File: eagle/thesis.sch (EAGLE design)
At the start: 18 parts, among them J1 RJ11-6PTH, U1 ITG-3200, U2 ADXL362

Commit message: wrote a bunch and added references and pictures
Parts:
- removed J1: RJ11-6PTH, SparkFun-Connectors:RJ11-6PTH
- removed U$4: SPARKFUN_HMC5883LSMD, HMC5883L_Breakout-v11:SPARKFUN_HMC5883LSMD
- added HMC5883L: SPARKFUN_HMC5883LSMD, HMC5883L_Breakout-v11:SPARKFUN_HMC5883LSMD
- added JHMR2300: RJ11-6PTH, SparkFun-Connectors:RJ11-6PTH
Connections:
- net 33V: now also C6.2, HMC5883L.S1, HMC5883L.VDD, HMC5883L.VDDIO, JHMR2300.2; no longer J1.2, U$4.S1, U$4.VDD, U$4.VDDIO
- net GND1_1: now also JHMR2300.1; no longer J1.1
- net GNDHEAD: now also HMC5883L.GND@1, HMC5883L.GND@2; no longer U$4.GND@1, U$4.GND@2
- net N$12: now also HMC5883L.C1; no longer U$4.C1
- net N$5: now also HMC5883L.SETP; no longer U$4.SETP
- net N$7: now also HMC5883L.SETC; no longer U$4.SETC
- net RX1: now also JHMR2300.3; no longer J1.3
- net SCL: now also HMC5883L.SCL; no longer U$4.SCL
- net SDA: now also HMC5883L.SDA; no longer U$4.SDA
- net TX1: now also JHMR2300.4; no longer J1.4
- net VIN: now also JHMR2300.5; no longer J1.5
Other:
- moved on the sheet: C1, C2, C3, C4, C5, C6, C7, R1, R2, U$3G$1, U1

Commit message: wrote more.
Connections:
- new net SCL1: U$1.SCL1, U1.SCL
- new net SDA1: U$1.SDA1, U1.SDA
- net 33V: now also JHMR2300.5; no longer JHMR2300.2
- net GND1_1: now also JHMR2300.6; no longer JHMR2300.1
- net RX1: now also JHMR2300.4; no longer JHMR2300.3
- net SCL: no longer U1.SCL
- net SDA: no longer U1.SDA
- net TX1: now also JHMR2300.3; no longer JHMR2300.4
- net VIN: now also JHMR2300.2; no longer JHMR2300.5
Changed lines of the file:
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@@
-</segment>
-<segment>
-<pinref part="JHMR2300" gate="G$1" pin="2"/>
-<wire x1="83.82" y1="78.74" x2="78.74" y2="78.74" width="0.1524" layer="91"/>
-<label x="81.28" y="78.74" size="1.778" layer="95" rot="R180"/>
 </segment>
 <segment>
@@
 <junction x="81.28" y="195.58"/>
 <label x="81.28" y="198.12" size="1.778" layer="95"/>
+</segment>
+<segment>
+<pinref part="JHMR2300" gate="G$1" pin="5"/>
+<wire x1="78.74" y1="86.36" x2="83.82" y2="86.36" width="0.1524" layer="91"/>
+<label x="76.2" y="86.36" size="1.778" layer="95"/>
 </segment>
 </net>
@@
 </segment>
 <segment>
-<pinref part="JHMR2300" gate="G$1" pin="5"/>
-<wire x1="83.82" y1="86.36" x2="78.74" y2="86.36" width="0.1524" layer="91"/>
-<label x="76.2" y="86.36" size="1.778" layer="95"/>
+<pinref part="JHMR2300" gate="G$1" pin="2"/>
+<wire x1="78.74" y1="78.74" x2="83.82" y2="78.74" width="0.1524" layer="91"/>
+<label x="76.2" y="78.74" size="1.778" layer="95"/>
 </segment>
 </net>
 <net name="TX1" class="0">
+<segment>
+<pinref part="U$1" gate="G$1" pin="TX1"/>
+<wire x1="-5.08" y1="45.72" x2="-2.54" y2="45.72" width="0.1524" layer="91"/>
+</segment>
+<segment>
+<pinref part="JHMR2300" gate="G$1" pin="3"/>
+<wire x1="83.82" y1="81.28" x2="78.74" y2="81.28" width="0.1524" layer="91"/>
+<label x="78.74" y="81.28" size="1.778" layer="95"/>
+</segment>
+</net>
+<net name="RX1" class="0">
+<segment>
+<pinref part="U$1" gate="G$1" pin="RX1"/>
+<wire x1="-2.54" y1="43.18" x2="-5.08" y2="43.18" width="0.1524" layer="91"/>
+</segment>
 <segment>
 <pinref part="JHMR2300" gate="G$1" pin="4"/>
 <wire x1="83.82" y1="83.82" x2="78.74" y2="83.82" width="0.1524" layer="91"/>
-<label x="81.28" y="83.82" size="1.778" layer="95" rot="R180"/>
-</segment>
-<segment>
-<pinref part="U$1" gate="G$1" pin="TX1"/>
-<wire x1="-5.08" y1="45.72" x2="-2.54" y2="45.72" width="0.1524" layer="91"/>
-</segment>
-</net>
-<net name="RX1" class="0">
-<segment>
-<pinref part="JHMR2300" gate="G$1" pin="3"/>
-<wire x1="78.74" y1="81.28" x2="83.82" y2="81.28" width="0.1524" layer="91"/>
-<label x="81.28" y="81.28" size="1.778" layer="95" rot="R180"/>
-</segment>
-<segment>
-<pinref part="U$1" gate="G$1" pin="RX1"/>
-<wire x1="-2.54" y1="43.18" x2="-5.08" y2="43.18" width="0.1524" layer="91"/>
+<label x="78.74" y="83.82" size="1.778" layer="95"/>
 </segment>
 </net>
@@
 <wire x1="-5.08" y1="58.42" x2="-2.54" y2="58.42" width="0.1524" layer="91"/>
 </segment>
-<segment>
-<pinref part="U1" gate="G$1" pin="SCL"/>
-<wire x1="50.8" y1="109.22" x2="45.72" y2="109.22" width="0.1524" layer="91"/>
-<label x="45.72" y="109.22" size="1.778" layer="95" rot="R180"/>
-</segment>
 </net>
 <net name="SDA" class="0">
@@
 <label x="2.54" y="157.48" size="1.778" layer="95" rot="R90"/>
 </segment>
-<segment>
-<pinref part="U1" gate="G$1" pin="SDA"/>
-<wire x1="50.8" y1="104.14" x2="45.72" y2="104.14" width="0.1524" layer="91"/>
-<label x="45.72" y="104.14" size="1.778" layer="95" rot="R180"/>
-</segment>
 </net>
 <net name="SCLK" class="0">
@@
 </segment>
 <segment>
-<pinref part="JHMR2300" gate="G$1" pin="1"/>
-<wire x1="83.82" y1="76.2" x2="78.74" y2="76.2" width="0.1524" layer="91"/>
-<label x="83.82" y="76.2" size="1.778" layer="95" rot="R180"/>
-</segment>
-<segment>
 <pinref part="U$6" gate="G$1" pin="GND"/>
 <wire x1="119.38" y1="76.2" x2="124.46" y2="76.2" width="0.1524" layer="91"/>
@@
 <wire x1="-7.62" y1="185.42" x2="-12.7" y2="185.42" width="0.1524" layer="91"/>
 <label x="-12.7" y="185.42" size="1.778" layer="95" rot="R180"/>
+</segment>
+<segment>
+<pinref part="JHMR2300" gate="G$1" pin="6"/>
+<wire x1="78.74" y1="88.9" x2="83.82" y2="88.9" width="0.1524" layer="91"/>
+<label x="76.2" y="88.9" size="1.778" layer="95"/>
 </segment>
 </net>
@@
 <pinref part="HMC5883L" gate="G$1" pin="GND@1"/>
 <wire x1="48.26" y1="175.26" x2="43.18" y2="175.26" width="0.1524" layer="91"/>
+<label x="40.64" y="175.26" size="1.778" layer="95"/>
 </segment>
 <segment>
 <pinref part="HMC5883L" gate="G$1" pin="GND@2"/>
 <wire x1="48.26" y1="172.72" x2="43.18" y2="172.72" width="0.1524" layer="91"/>
-</segment>
-</net>
+<label x="40.64" y="172.72" size="1.778" layer="95"/>
+</segment>
+</net>
+<net name="SCL1" class="0">
+<segment>
+<pinref part="U$1" gate="G$1" pin="SCL1"/>
+<wire x1="7.62" y1="86.36" x2="7.62" y2="91.44" width="0.1524" layer="91"/>
+</segment>
+<segment>
+<pinref part="U1" gate="G$1" pin="SCL"/>
+<wire x1="50.8" y1="109.22" x2="45.72" y2="109.22" width="0.1524" layer="91"/>
+<label x="45.72" y="109.22" size="1.778" layer="95" rot="R180"/>
+</segment>
+</net>
+<net name="SDA1" class="0">
+<segment>
+<pinref part="U$1" gate="G$1" pin="SDA1"/>
+<wire x1="10.16" y1="86.36" x2="10.16" y2="91.44" width="0.1524" layer="91"/>
+</segment>
+<segment>
+<pinref part="U1" gate="G$1" pin="SDA"/>
+<wire x1="50.8" y1="104.14" x2="45.72" y2="104.14" width="0.1524" layer="91"/>
+<label x="45.72" y="104.14" size="1.778" layer="95" rot="R180"/>
+</segment>
+</net>

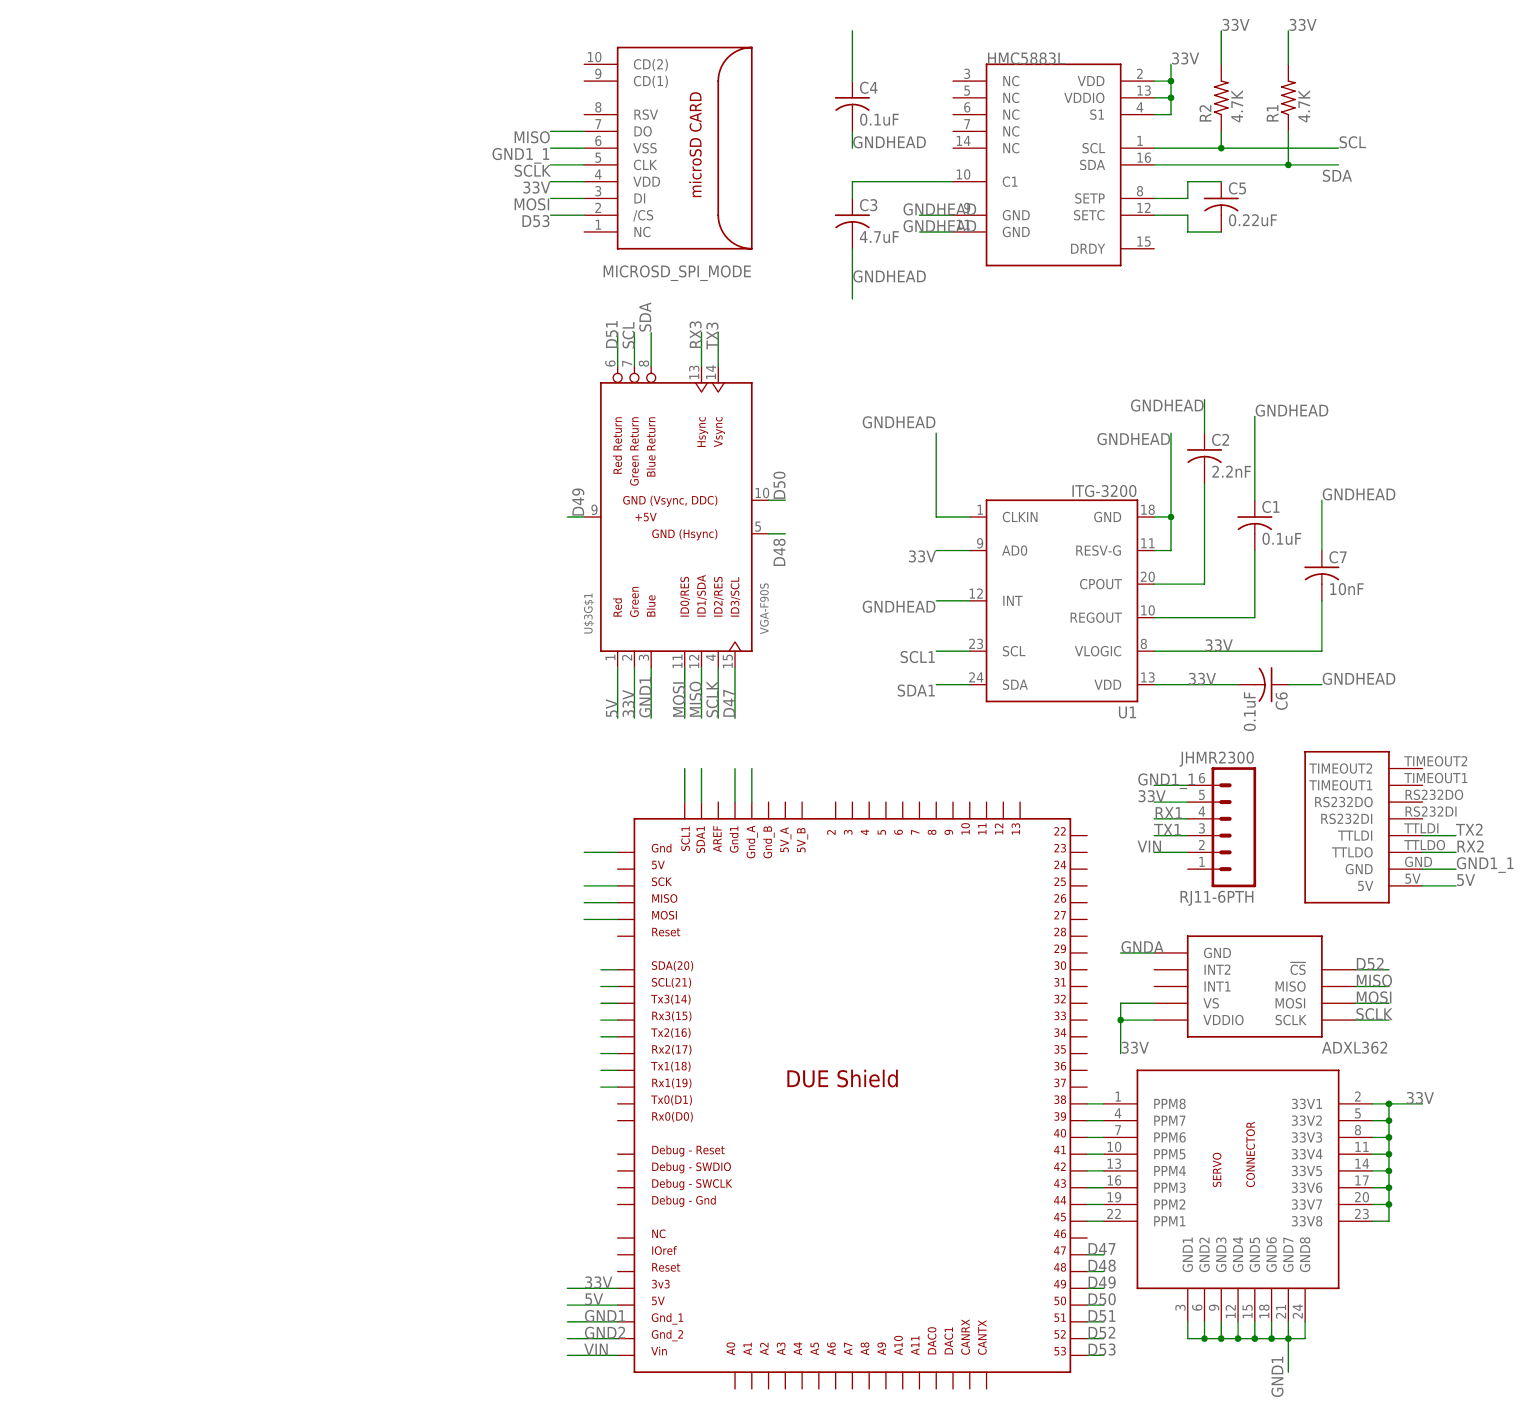
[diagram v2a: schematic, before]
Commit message: changed eagle files.
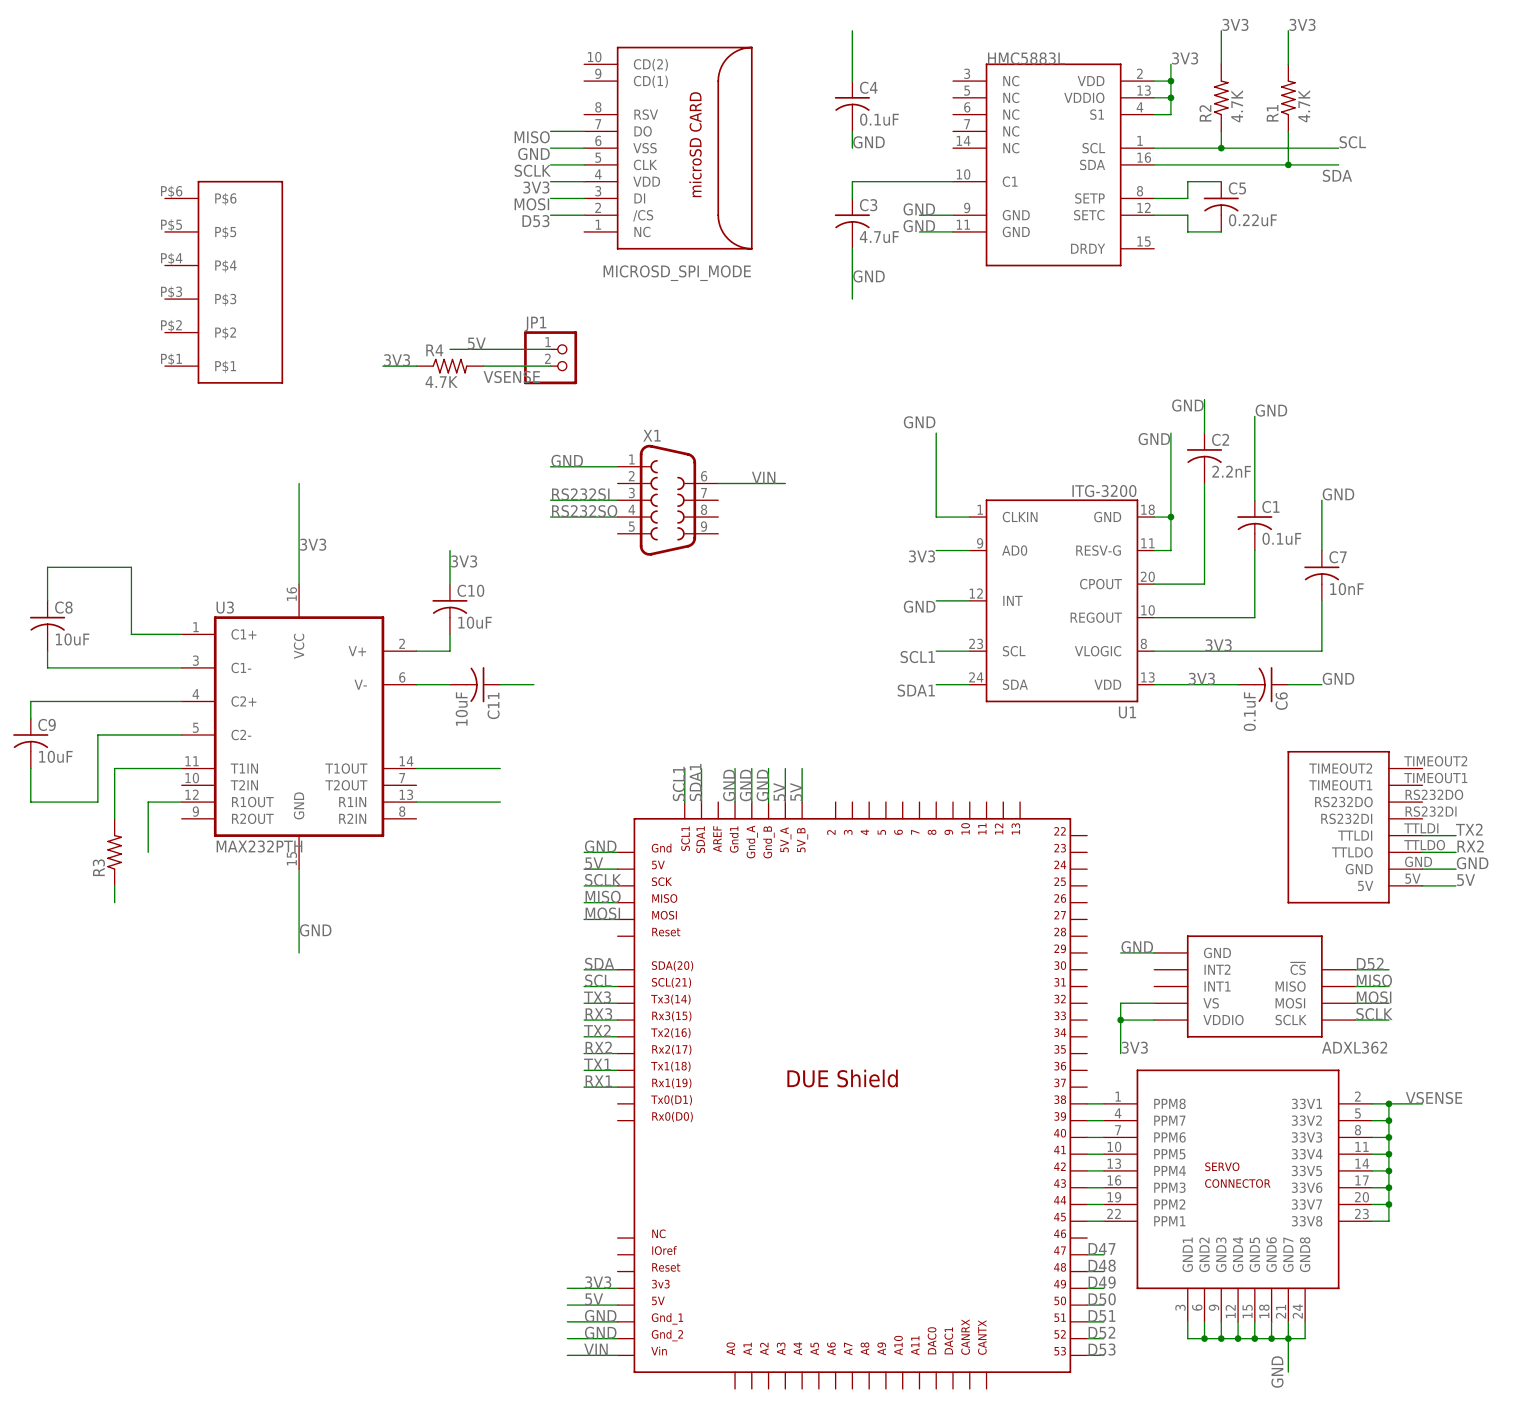
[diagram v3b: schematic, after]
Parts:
- removed JHMR2300: RJ11-6PTH, SparkFun-Connectors:RJ11-6PTH
- added C10, C11, C8, C9: 10uF, rcl:C-USC0603K
- added JP1: (no value), pinhead:PINHD-1X2
- added R3: (no value), rcl:R-US_R0603
- added R4: 4.7K, rcl:R-US_R0603
- added U3: MAX232PTH, SparkFun-DigitalIC:MAX232PTH
- added X1: (no value), con-subd:F09VP
- U$3: value VGA-F90S -> RJ11V; device VideoConnectors:VGA-F90S -> RJ11V:RJ11V
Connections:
- removed net 33V: C4.1, C6.2, C7.2, HMC5883L.S1, HMC5883L.VDD, HMC5883L.VDDIO, JHMR2300.5, R1.2, R2.2, U$1.3V3, U$2.VDD, U$3G$1.VGA-G, U$5.33V1, U$5.33V2, U$5.33V3, U$5.33V4, U$5.33V5, U$5.33V6, U$5.33V7, U$5.33V8, U1.AD0, U1.VDD, U1.VLOGIC, U2.VDDIO, U2.VS
- removed net GND1: U$1.GND_1, U$3G$1.VGA-B, U$5.GND1, U$5.GND2, U$5.GND3, U$5.GND4, U$5.GND5, U$5.GND6, U$5.GND7, U$5.GND8
- removed net GND1_1: JHMR2300.6, U$1.GND1, U$2.VSS, U$6.GND
- removed net GND2: U$1.GND_2
- removed net GNDA: U$1.GND_A, U2.GND
- removed net GNDHEAD: C1.1, C2.1, C3.2, C4.2, C6.1, C7.1, HMC5883L.GND@1, HMC5883L.GND@2, U$1.5V_ICSP, U1.CLKIN, U1.GND, U1.INT, U1.RESV-G
- new net 3V3: C10.1, C4.1, C6.2, C7.2, HMC5883L.S1, HMC5883L.VDD, HMC5883L.VDDIO, R1.2, R2.2, R3.1, R4.1, U$1.3V3, U$2.VDD, U1.AD0, U1.VDD, U1.VLOGIC, U2.VDDIO, U2.VS, U3.VCC
- new net GND: C1.1, C11.1, C2.1, C3.2, C4.2, C6.1, C7.1, HMC5883L.GND@1, HMC5883L.GND@2, U$1.5V_ICSP, U$1.GND1, U$1.GND_1, U$1.GND_2, U$1.GND_A, U$1.GND_B, U$2.VSS, U$5.GND1, U$5.GND2, U$5.GND3, U$5.GND4, U$5.GND5, U$5.GND6, U$5.GND7, U$5.GND8, U$6.GND, U1.CLKIN, U1.GND, U1.INT, U1.RESV-G, U2.GND, U3.GND, X1.1
- new net N$1: C10.2, U3.V+
- new net N$2: C11.2, U3.V-
- new net N$3: C9.1, U3.C2+
- new net N$4: C9.2, U3.C2-
- new net N$6: C8.1, U3.C1+
- new net N$8: C8.2, U3.C1-
- new net RS232SI: U3.T1OUT, X1.3
- new net RS232SO: U3.R1IN, X1.4
- new net VSENSE: JP1.2, R4.2, U$5.33V1, U$5.33V2, U$5.33V3, U$5.33V4, U$5.33V5, U$5.33V6, U$5.33V7, U$5.33V8
- net 5V: now also JP1.1, U$1.5V_A, U$1.5V_B, U$1.GND_ICSP; no longer U$3G$1.VGA-R
- net D47: no longer U$3G$1.ID3/SCL
- net D48: no longer U$3G$1.GND@0
- net D49: no longer U$3G$1.+5V
- net D50: no longer U$3G$1.GND@1
- net D51: no longer U$3G$1.VGA-R-
- net MISO: no longer U$3G$1.ID1/SDA
- net MOSI: no longer U$3G$1.ID0/RES
- net RX1: now also U3.R1OUT; no longer JHMR2300.4
- net RX3: no longer U$3G$1.VGA-HSYNC
- net SCL: no longer U$3G$1.VGA-G-
- net SCLK: no longer U$3G$1.ID2/RES
- net SDA: no longer U$3G$1.VGA-B-
- net TX1: now also R3.2, U3.T1IN; no longer JHMR2300.3
- net TX3: no longer U$3G$1.VGA-VSYNC
- net VIN: now also X1.6; no longer JHMR2300.2

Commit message: modified eagle boards and ordered.
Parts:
- added Q1, Q3: BSS138, SparkFun-DiscreteSemi:MOSFET-NCHANNELBSS123LT1G
- added R10, R11, R5, R6, R7, R9: 10K, rcl:R-US_R0603
- added R12, R8: 20K, rcl:R-US_R0603
- R3: value (none) -> 1K
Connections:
- removed net SCL: HMC5883L.SCL, R2.1, U$1.SCL
- removed net SDA: HMC5883L.SDA, R1.1, U$1.SDA
- new net RX2H: R11.2, U$6.TTLDO
- new net RX3H: R7.2, U$3.P$5
- new net TX2H: Q1.D, R10.1, U$6.TTLDI
- new net TX3H: Q3.D, R6.1, U$3.P$2
- net 3V3: now also Q1.G, Q3.G, R5.2, R9.2
- net 5V: now also R10.2, R6.2, U$3.P$3
- net GND: now also R12.1, R8.1, U$3.P$6; no longer U1.INT
- net RX2: now also R11.1, R12.2; no longer U$6.TTLDO
- net RX3: now also R7.1, R8.2
- net SCL1: now also HMC5883L.SCL, R2.1, U$1.SCL
- net SDA1: now also HMC5883L.SDA, R1.1, U$1.SDA
- net TX2: now also Q1.S, R9.1; no longer U$6.TTLDI
- net TX3: now also Q3.S, R5.1
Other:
- moved on the sheet: C1, C10, C11, C2, C6, C7, C8, C9, JP1, R3, R4, U1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
